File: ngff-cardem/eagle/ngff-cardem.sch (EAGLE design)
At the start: 147 parts, among them IC1 FPF2109, IC2 FPF2109, IC201 CB3Q3244PW, IC202 CB3Q3244PW, IC203 IP4234CZ6, IC301 MCP1703CB, IC302 TPS22958-DGN, J301 PJ-002BH-SMT-TR, M2 MENTOR_12701001, M3 MENTOR_12701001, Q201 12MHz, T101 BC847, U201 IP4234CZ6, U202 AT91SAM3S-AU, U301 MIC5366-1.8YC5, X1 PINHD-2X3-SP, X102 ZX360D-B-10P(30), X2 PINHD-2X3-SP, X201 MINI-USB-SHIELD-UX60-MB-5ST, X202 2.54mm, X3 JACK2.5_SJ-2523, X301 22-23-2041

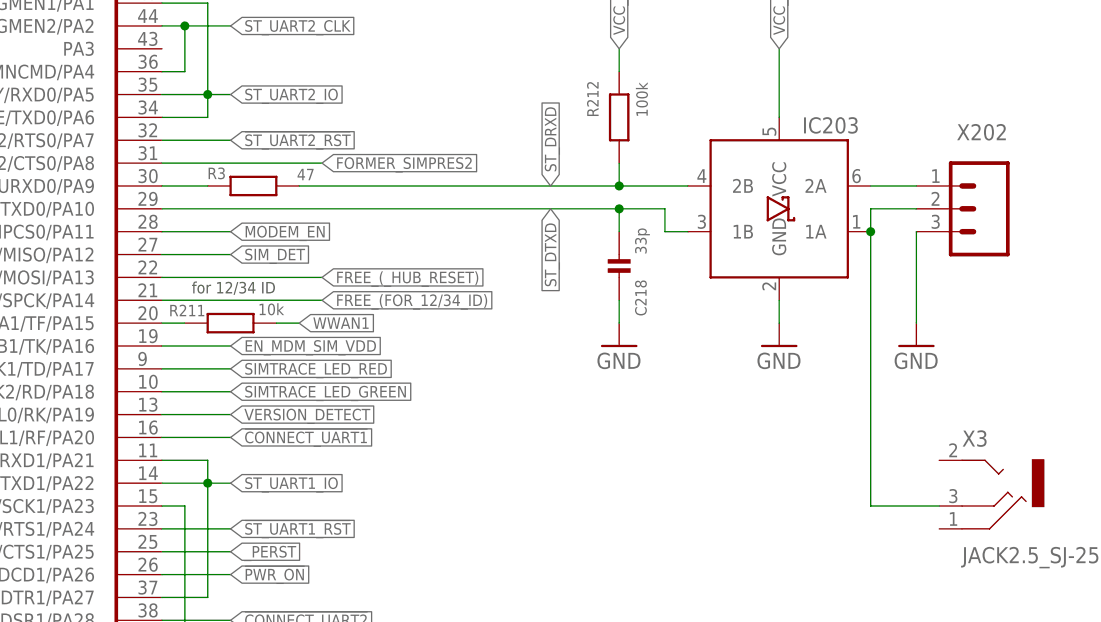
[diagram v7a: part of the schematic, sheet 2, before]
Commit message: ngff-cardem: add 2.5mm stereo jack for debug UART (solves SYS#5471)
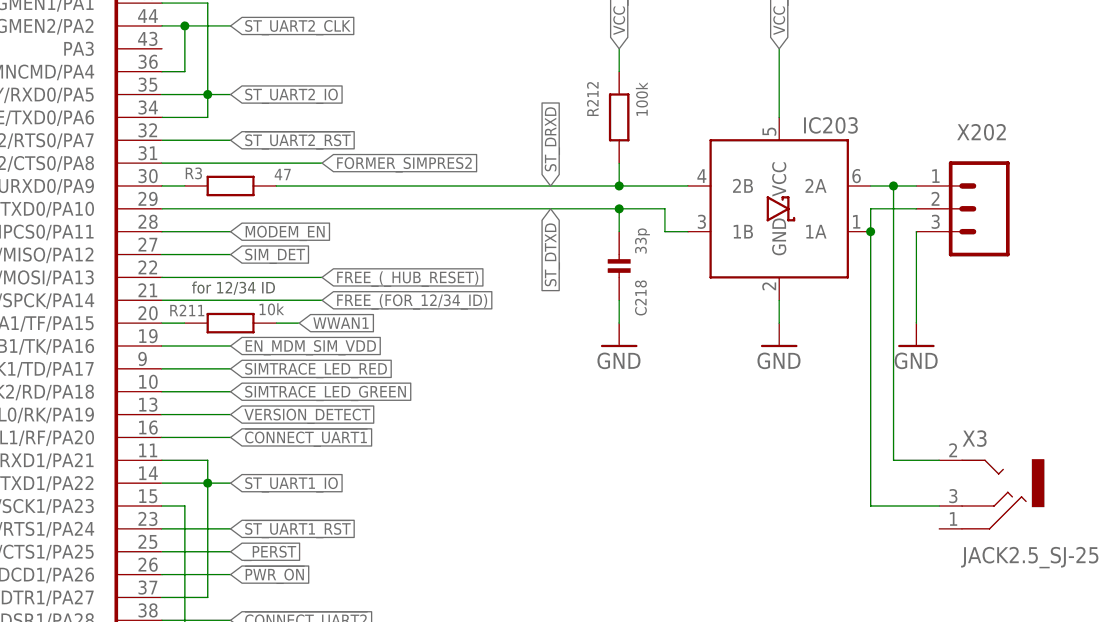
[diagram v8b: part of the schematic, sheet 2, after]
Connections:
- net N$68: now also X3.TIP
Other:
- moved on the sheet: R3
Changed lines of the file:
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@@
 <attribute name="LINK" x="297.18" y="175.26" size="1.778" layer="96" display="off"/>
 </instance>
-<instance part="R3" gate="G$1" x="215.9" y="208.28" smashed="yes">
-<attribute name="NAME" x="212.852" y="210.312" size="1.27" layer="95" rot="R180"/>
-<attribute name="VALUE" x="220.726" y="208.915" size="1.27" layer="96"/>
-<attribute name="DESCRIPTION" x="215.9" y="208.28" size="1.778" layer="96" rot="R180" display="off"/>
-<attribute name="MANUFACTURER" x="215.9" y="208.28" size="1.778" layer="96" rot="R180" display="off"/>
-<attribute name="MANUFACTURERPARTNUMBER" x="215.9" y="208.28" size="1.778" layer="96" rot="R180" display="off"/>
-<attribute name="SOURCE" x="215.9" y="208.28" size="1.778" layer="96" rot="R180" display="off"/>
-<attribute name="SOURCEPARTNUMBER" x="215.9" y="208.28" size="1.778" layer="96" rot="R180" display="off"/>
-<attribute name="ROHSCERTIFICATE" x="215.9" y="208.28" size="1.778" layer="96" rot="R180" display="off"/>
-<attribute name="POPULATED" x="215.9" y="208.28" size="1.778" layer="96" rot="R180" display="off"/>
-<attribute name="CLASS" x="215.9" y="208.28" size="1.778" layer="96" rot="R180" display="off"/>
-<attribute name="LINK" x="215.9" y="208.28" size="1.778" layer="96" rot="R180" display="off"/>
+<instance part="R3" gate="G$1" x="213.36" y="208.28" smashed="yes">
+<attribute name="NAME" x="210.312" y="210.312" size="1.27" layer="95" rot="R180"/>
+<attribute name="VALUE" x="218.186" y="208.915" size="1.27" layer="96"/>
+<attribute name="DESCRIPTION" x="213.36" y="208.28" size="1.778" layer="96" rot="R180" display="off"/>
+<attribute name="MANUFACTURER" x="213.36" y="208.28" size="1.778" layer="96" rot="R180" display="off"/>
+<attribute name="MANUFACTURERPARTNUMBER" x="213.36" y="208.28" size="1.778" layer="96" rot="R180" display="off"/>
+<attribute name="SOURCE" x="213.36" y="208.28" size="1.778" layer="96" rot="R180" display="off"/>
+<attribute name="SOURCEPARTNUMBER" x="213.36" y="208.28" size="1.778" layer="96" rot="R180" display="off"/>
+<attribute name="ROHSCERTIFICATE" x="213.36" y="208.28" size="1.778" layer="96" rot="R180" display="off"/>
+<attribute name="POPULATED" x="213.36" y="208.28" size="1.778" layer="96" rot="R180" display="off"/>
+<attribute name="CLASS" x="213.36" y="208.28" size="1.778" layer="96" rot="R180" display="off"/>
+<attribute name="LINK" x="213.36" y="208.28" size="1.778" layer="96" rot="R180" display="off"/>
 </instance>
 </instances>
@@
 <wire x1="256.54" y1="208.28" x2="264.16" y2="208.28" width="0.1524" layer="91"/>
 <pinref part="R3" gate="G$1" pin="2"/>
-<wire x1="220.98" y1="208.28" x2="256.54" y2="208.28" width="0.1524" layer="91"/>
+<wire x1="218.44" y1="208.28" x2="256.54" y2="208.28" width="0.1524" layer="91"/>
 <junction x="256.54" y="208.28"/>
 </segment>
@@
 <pinref part="IC203" gate="G$1" pin="2A"/>
 <pinref part="X202" gate="G$1" pin="1"/>
-<wire x1="284.48" y1="208.28" x2="289.56" y2="208.28" width="0.1524" layer="91"/>
+<wire x1="284.48" y1="208.28" x2="287.02" y2="208.28" width="0.1524" layer="91"/>
+<pinref part="X3" gate="G$1" pin="TIP"/>
+<wire x1="287.02" y1="208.28" x2="289.56" y2="208.28" width="0.1524" layer="91"/>
+<wire x1="292.1" y1="177.8" x2="287.02" y2="177.8" width="0.1524" layer="91"/>
+<wire x1="287.02" y1="177.8" x2="287.02" y2="208.28" width="0.1524" layer="91"/>
+<junction x="287.02" y="208.28"/>
 </segment>
 </net>
@@
 <pinref part="R3" gate="G$1" pin="1"/>
 <pinref part="U202" gate="G$1" pin="NPCS1/URXD0/PA9"/>
-<wire x1="210.82" y1="208.28" x2="205.74" y2="208.28" width="0.1524" layer="91"/>
-</segment>
-</net>
+<wire x1="208.28" y1="208.28" x2="205.74" y2="208.28" width="0.1524" layer="91"/>
+</segment>
+</net>
